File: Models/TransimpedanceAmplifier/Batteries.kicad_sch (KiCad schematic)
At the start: 16 parts, among them J12 Keystone_968, J14 Keystone_968, J15 Keystone_968, J16 Keystone_968, J17 Keystone_968, J18 Keystone_968, J20 Keystone_968, J21 Keystone_968

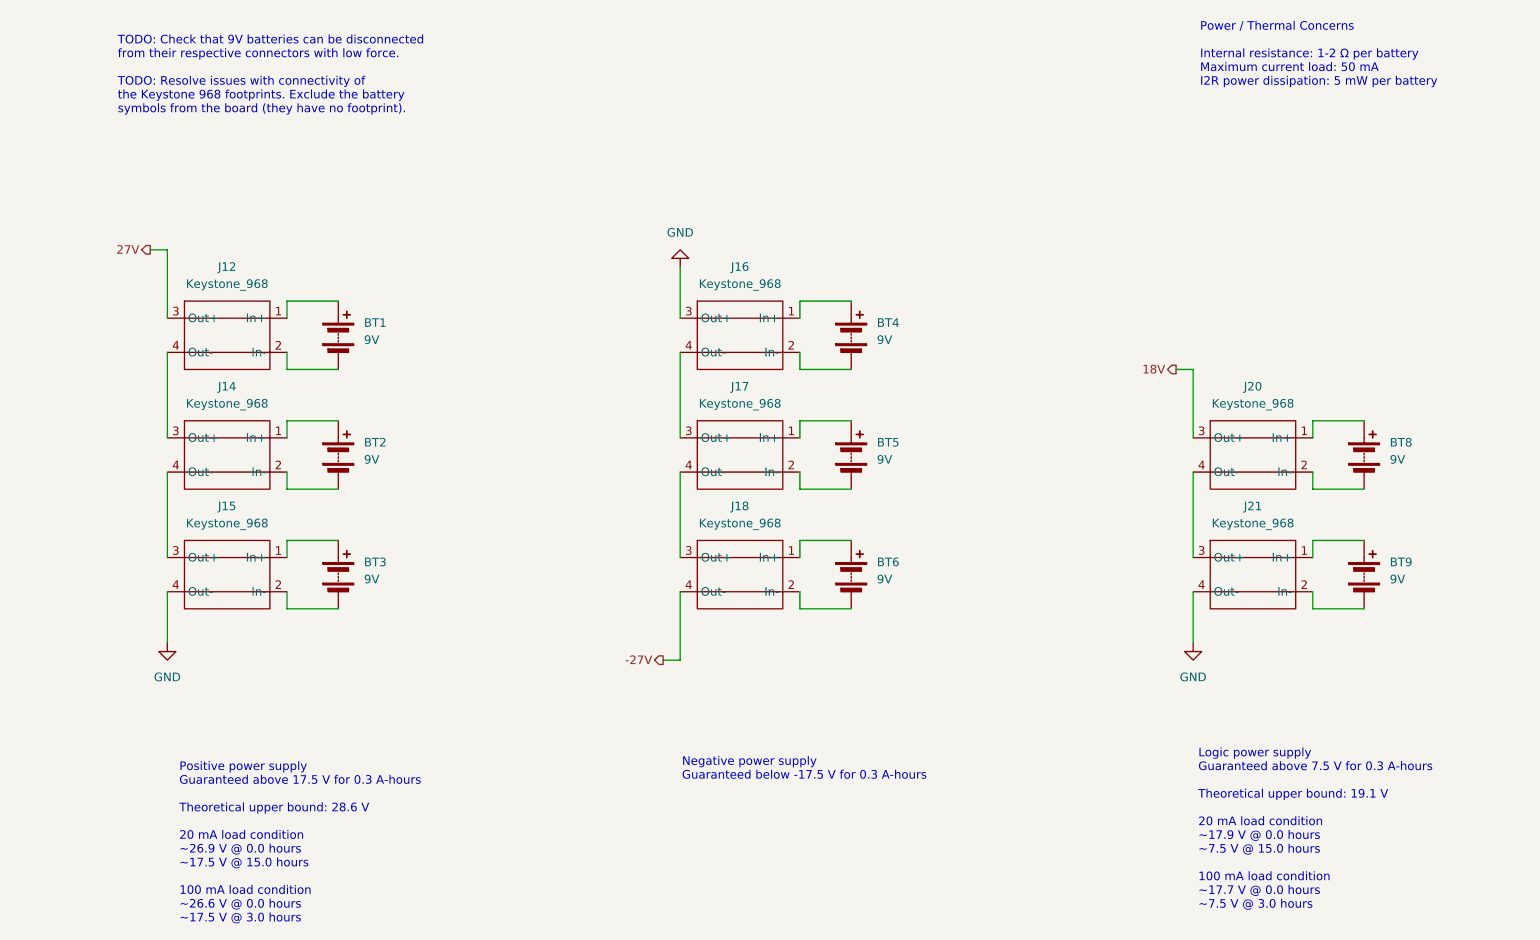
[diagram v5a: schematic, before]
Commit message: Overhauled all of the annotations
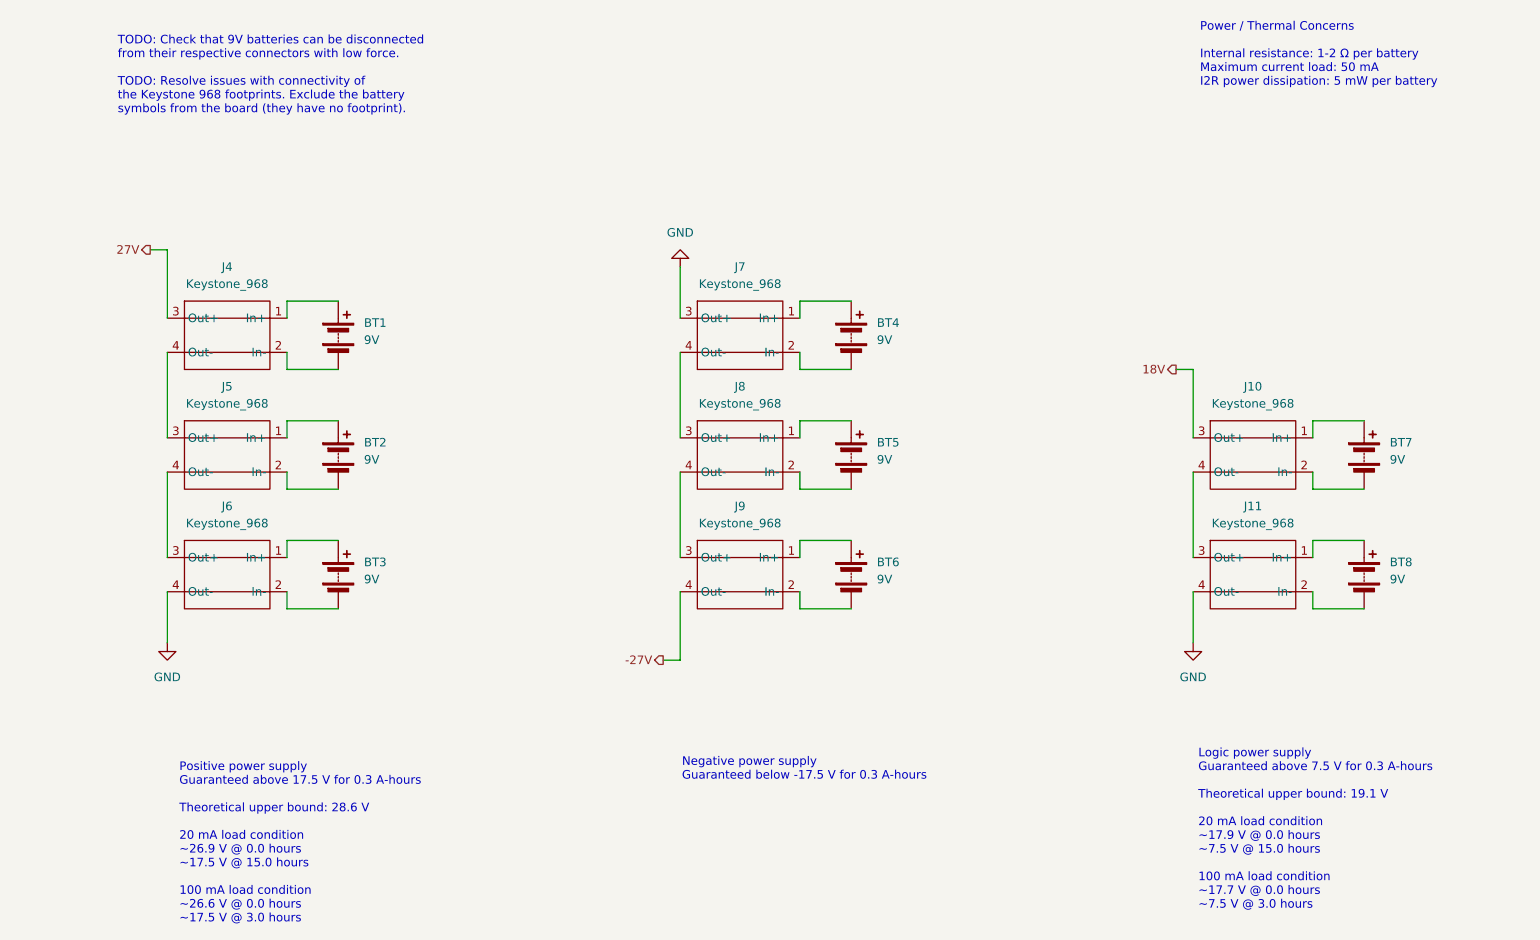
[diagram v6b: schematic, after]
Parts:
- renumbered BT8 to BT7, BT9 to BT8, J20 to J10, J21 to J11, J12 to J4, J14 to J5, J15 to J6, J16 to J7, J17 to J8, J18 to J9
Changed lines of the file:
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@@
 		(on_board yes)
 		(dnp no)
-		(property "Reference" "J12"
+		(property "Reference" "J4"
 			(at 59.69 63.5 0)
 			(effects
@@
 			(project ""
 				(path "/ec9f2ae3-e40d-40eb-9760-2b611ee8efd1/d0ece2d4-5b22-4822-ad0c-e2361683ec3d/c9cd3b70-0193-478b-9c9b-cf8238587205"
-					(reference "J12")
+					(reference "J4")
 					(unit 1)
 				)
@@
 		(dnp no)
 		(fields_autoplaced yes)
-		(property "Reference" "BT8"
+		(property "Reference" "BT7"
 			(at 232.41 89.5984 0)
 			(effects
@@
 			(project "TransimpedanceAmplifier"
 				(path "/ec9f2ae3-e40d-40eb-9760-2b611ee8efd1/d0ece2d4-5b22-4822-ad0c-e2361683ec3d/c9cd3b70-0193-478b-9c9b-cf8238587205"
-					(reference "BT8")
+					(reference "BT7")
 					(unit 1)
 				)
@@
 		(dnp no)
 		(fields_autoplaced yes)
-		(property "Reference" "#PWR016"
+		(property "Reference" "#PWR02"
 			(at 127 57.15 0)
 			(effects
@@
 			(project ""
 				(path "/ec9f2ae3-e40d-40eb-9760-2b611ee8efd1/d0ece2d4-5b22-4822-ad0c-e2361683ec3d/c9cd3b70-0193-478b-9c9b-cf8238587205"
-					(reference "#PWR016")
+					(reference "#PWR02")
 					(unit 1)
 				)
@@
 		(on_board yes)
 		(dnp no)
-		(property "Reference" "J14"
+		(property "Reference" "J5"
 			(at 59.69 81.28 0)
 			(effects
@@
 			(project "TransimpedanceAmplifier"
 				(path "/ec9f2ae3-e40d-40eb-9760-2b611ee8efd1/d0ece2d4-5b22-4822-ad0c-e2361683ec3d/c9cd3b70-0193-478b-9c9b-cf8238587205"
-					(reference "J14")
+					(reference "J5")
 					(unit 1)
 				)
@@
 		(on_board yes)
 		(dnp no)
-		(property "Reference" "J16"
+		(property "Reference" "J7"
 			(at 135.89 63.5 0)
 			(effects
@@
 			(project "TransimpedanceAmplifier"
 				(path "/ec9f2ae3-e40d-40eb-9760-2b611ee8efd1/d0ece2d4-5b22-4822-ad0c-e2361683ec3d/c9cd3b70-0193-478b-9c9b-cf8238587205"
-					(reference "J16")
+					(reference "J7")
 					(unit 1)
 				)
@@
 		(on_board yes)
 		(dnp no)
-		(property "Reference" "J21"
+		(property "Reference" "J11"
 			(at 212.09 99.06 0)
 			(effects
@@
 			(project "TransimpedanceAmplifier"
 				(path "/ec9f2ae3-e40d-40eb-9760-2b611ee8efd1/d0ece2d4-5b22-4822-ad0c-e2361683ec3d/c9cd3b70-0193-478b-9c9b-cf8238587205"
-					(reference "J21")
+					(reference "J11")
 					(unit 1)
 				)
@@
 		(dnp no)
 		(fields_autoplaced yes)
-		(property "Reference" "BT9"
+		(property "Reference" "BT8"
 			(at 232.41 107.3784 0)
 			(effects
@@
 			(project "TransimpedanceAmplifier"
 				(path "/ec9f2ae3-e40d-40eb-9760-2b611ee8efd1/d0ece2d4-5b22-4822-ad0c-e2361683ec3d/c9cd3b70-0193-478b-9c9b-cf8238587205"
-					(reference "BT9")
+					(reference "BT8")
 					(unit 1)
 				)
@@
 		(on_board yes)
 		(dnp no)
-		(property "Reference" "J20"
+		(property "Reference" "J10"
 			(at 212.09 81.28 0)
 			(effects
@@
 			(project "TransimpedanceAmplifier"
 				(path "/ec9f2ae3-e40d-40eb-9760-2b611ee8efd1/d0ece2d4-5b22-4822-ad0c-e2361683ec3d/c9cd3b70-0193-478b-9c9b-cf8238587205"
-					(reference "J20")
+					(reference "J10")
 					(unit 1)
 				)
@@
 		(on_board yes)
 		(dnp no)
-		(property "Reference" "J17"
+		(property "Reference" "J8"
 			(at 135.89 81.28 0)
 			(effects
@@
 			(project "TransimpedanceAmplifier"
 				(path "/ec9f2ae3-e40d-40eb-9760-2b611ee8efd1/d0ece2d4-5b22-4822-ad0c-e2361683ec3d/c9cd3b70-0193-478b-9c9b-cf8238587205"
-					(reference "J17")
+					(reference "J8")
 					(unit 1)
 				)
@@
 		(on_board yes)
 		(dnp no)
-		(property "Reference" "J15"
+		(property "Reference" "J6"
 			(at 59.69 99.06 0)
 			(effects
@@
 			(project "TransimpedanceAmplifier"
 				(path "/ec9f2ae3-e40d-40eb-9760-2b611ee8efd1/d0ece2d4-5b22-4822-ad0c-e2361683ec3d/c9cd3b70-0193-478b-9c9b-cf8238587205"
-					(reference "J15")
+					(reference "J6")
 					(unit 1)
 				)
@@
 		(dnp no)
 		(fields_autoplaced yes)
-		(property "Reference" "#PWR013"
+		(property "Reference" "#PWR01"
 			(at 50.8 125.73 0)
 			(effects
@@
 			(project ""
 				(path "/ec9f2ae3-e40d-40eb-9760-2b611ee8efd1/d0ece2d4-5b22-4822-ad0c-e2361683ec3d/c9cd3b70-0193-478b-9c9b-cf8238587205"
-					(reference "#PWR013")
+					(reference "#PWR01")
 					(unit 1)
 				)
@@
 		(on_board yes)
 		(dnp no)
-		(property "Reference" "J18"
+		(property "Reference" "J9"
 			(at 135.89 99.06 0)
 			(effects
@@
 			(project "TransimpedanceAmplifier"
 				(path "/ec9f2ae3-e40d-40eb-9760-2b611ee8efd1/d0ece2d4-5b22-4822-ad0c-e2361683ec3d/c9cd3b70-0193-478b-9c9b-cf8238587205"
-					(reference "J18")
+					(reference "J9")
 					(unit 1)
 				)
@@
 		(dnp no)
 		(fields_autoplaced yes)
-		(property "Reference" "#PWR055"
+		(property "Reference" "#PWR03"
 			(at 203.2 125.73 0)
 			(effects
@@
 			(project ""
 				(path "/ec9f2ae3-e40d-40eb-9760-2b611ee8efd1/d0ece2d4-5b22-4822-ad0c-e2361683ec3d/c9cd3b70-0193-478b-9c9b-cf8238587205"
-					(reference "#PWR055")
-					(unit 1)
-				)
+					(reference "#PWR03")
+					(unit 1)
+				)

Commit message: Completely fixed the batteries
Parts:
- removed BT1, BT2, BT3, BT4, BT5, BT6, BT7, BT8: 9V, symbol Device:Battery
- removed J10, J11, J4, J5, J6, J7, J8, J9: Keystone_968, symbol Custom:Keystone_968
- added BT1, BT2: BatteryModule, symbol Custom:BatteryModule
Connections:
- net -27V: now also BT2.8 (BT4(-))
- net 18V: now also BT1.7 (BT4(+))
- net 27V: now also BT1.5 (BT3(+))
- net GND: now also BT1.4 (BT2(-)), BT2.1 (BT1(+)), BT2.6 (BT3(-))
- new net: BT1.1 (BT1(+)), BT1.6 (BT3(-))
- new net: BT1.2 (BT1(-)), BT1.3 (BT2(+))
- new net: BT1.8 (BT4(-)), BT2.5 (BT3(+))
- new net: BT2.2 (BT1(-)), BT2.3 (BT2(+))
- new net: BT2.4 (BT2(-)), BT2.7 (BT4(+))
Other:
- note added: "6 hour lifetime easily exceeded during a long debugging session; order a spare 8-pack of 9 V batteries"
- note removed: "TODO: Check that 9V batteries can be disconnected from their respective connectors with low force. TODO: Resolve issues with connectivity of the Keystone 968 footprints. Exclude the battery symbols from the board (they have no footprint)."

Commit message: Working on filling in the last details of the schematics
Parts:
- BT1, BT2: footprint (none) -> Connector_Custom:BatteryModule; Cost (none) -> $0.00; RoHS Compliant (none) -> NO
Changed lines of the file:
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@@
 			)
 		)
-		(property "Footprint" ""
+		(property "Footprint" "Connector_Custom:BatteryModule"
 			(at 170.18 62.23 0)
 			(effects
@@
 		)
 		(property "Description" ""
+			(at 170.18 62.23 0)
+			(effects
+				(font
+					(size 1.27 1.27)
+				)
+				(hide yes)
+			)
+		)
+		(property "Cost" "$0.00"
+			(at 170.18 62.23 0)
+			(effects
+				(font
+					(size 1.27 1.27)
+				)
+				(hide yes)
+			)
+		)
+		(property "RoHS Compliant" "NO"
 			(at 170.18 62.23 0)
 			(effects
@@
 			)
 		)
-		(property "Footprint" ""
+		(property "Footprint" "Connector_Custom:BatteryModule"
 			(at 170.18 110.49 0)
 			(effects
@@
 			(at 170.18 110.49 0)
 			(effects
+				(font
+					(size 1.27 1.27)
+				)
+				(hide yes)
+			)
+		)
+		(property "Cost" "$0.00"
+			(at 170.18 110.49 0)
+			(effects
+				(font
+					(size 1.27 1.27)
+				)
+				(hide yes)
+			)
+		)
+		(property "RoHS Compliant" "NO"
+			(at 170.18 110.49 0)
+			(effects
